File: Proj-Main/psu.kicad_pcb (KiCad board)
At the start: 2 copper layers, 100 x 75 mm, 124 parts, among them J1 METER, J3 T1A, J4 T1B, J5 T1C, J6 SENSE, J8 OUT+, J9 OUT-, Q1 BC856, Q10 BC856, Q11 PMP4201Y, Q12 MMBT3904, Q13 BC856, Q14 MMBT3904, Q15 PZT2222A, Q16 MMBT3904, Q17 TIP105, Q18 PMP4201Y, Q19 MMBT2907A, Q2 MMBT3904, Q20 MMBT2907A, Q21 MMBT2907A, Q22 MMBT3904, Q23 PMP4201Y, Q24 MMBT3904, Q3 PZT2222A, Q4 BC856, Q5 MMBT3906, Q6 MMBT3906, Q7 PMP4201Y, Q8 PMP4201Y, Q9 BC856

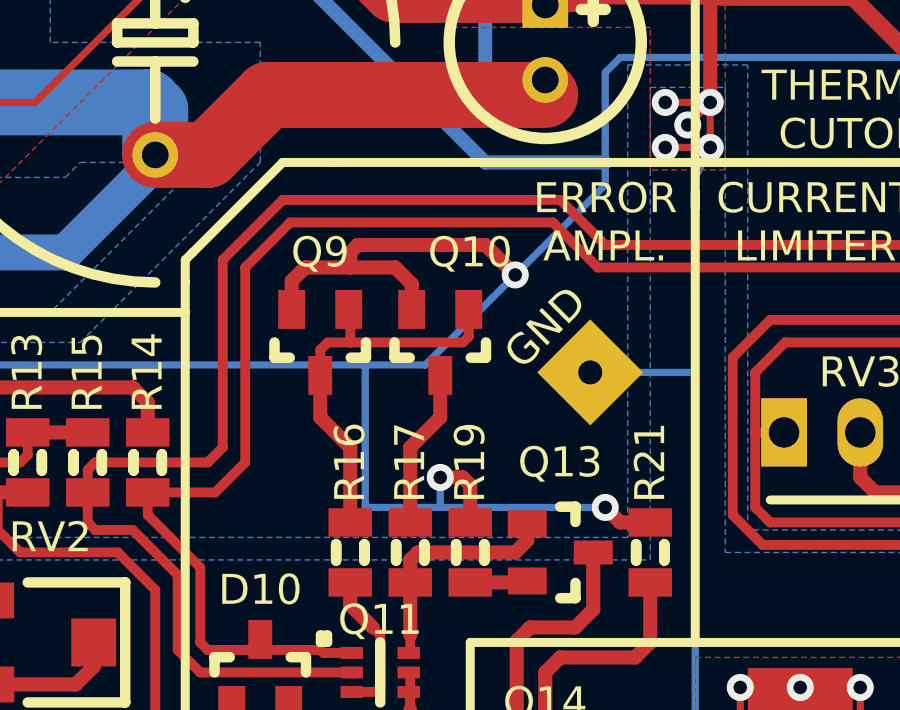
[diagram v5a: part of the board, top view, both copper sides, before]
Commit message: Added current mirror degeneration resistors R54, R55
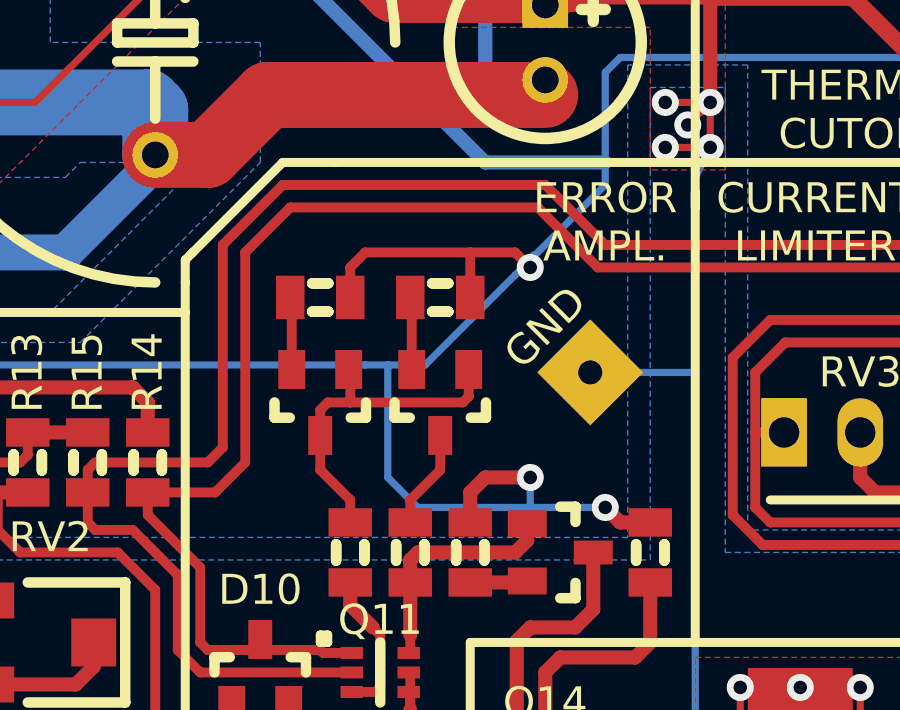
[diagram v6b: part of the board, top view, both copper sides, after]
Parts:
- added R54: 100, IPC7351-Nominal:RESC2012X50, F.Cu at (160.0, 86.5)
- added R55: 100, IPC7351-Nominal:RESC2012X50, F.Cu at (164.0, 86.5)
- moved Q10 2.00 mm to (164.0, 90.0)
- moved Q9 2.00 mm to (160.0, 90.0)
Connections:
- Q10 pad 2: V+ -> Net-(Q10-Pad2)
- Q9 pad 2: V+ -> Net-(Q9-Pad2)
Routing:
- net V+: track 278.0 -> 273.6 mm
- net Net-(Q9-Pad2): track 0.00 -> 2.42 mm
- net Net-(Q10-Pad2): track 0.00 -> 2.42 mm
- net Net-(Q10-Pad1): track 13.4 -> 11.3 mm
- net Net-(Q10-Pad3): track 5.31 -> 3.31 mm
- net /FB+: track 95.1 -> 95.8 mm
- net /FB-: track 89.5 -> 90.2 mm

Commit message: Renamed voltage rails (V+ and V- now +2 and -12)
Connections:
- net V+ renamed +2
- net V- renamed -12
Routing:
- added copper zone on B.Cu, net V+
- added copper zone on F.Cu, net V+
- added copper zone on B.Cu, net V-
- added copper zone on F.Cu, net V-
- removed copper zone on B.Cu, net +2
- removed copper zone on F.Cu, net +2
- removed copper zone on B.Cu, net -12
- removed copper zone on F.Cu, net -12

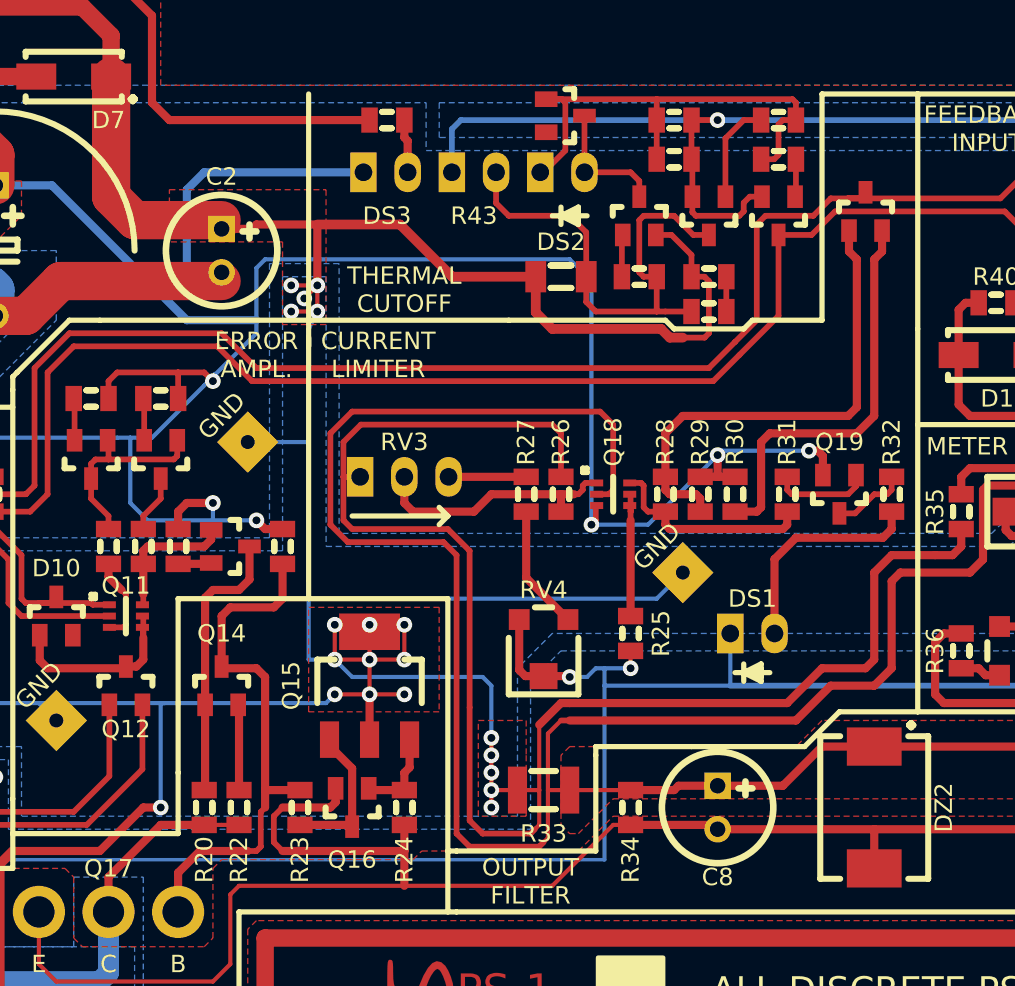
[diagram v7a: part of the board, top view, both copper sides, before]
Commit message: Updated LED bias points
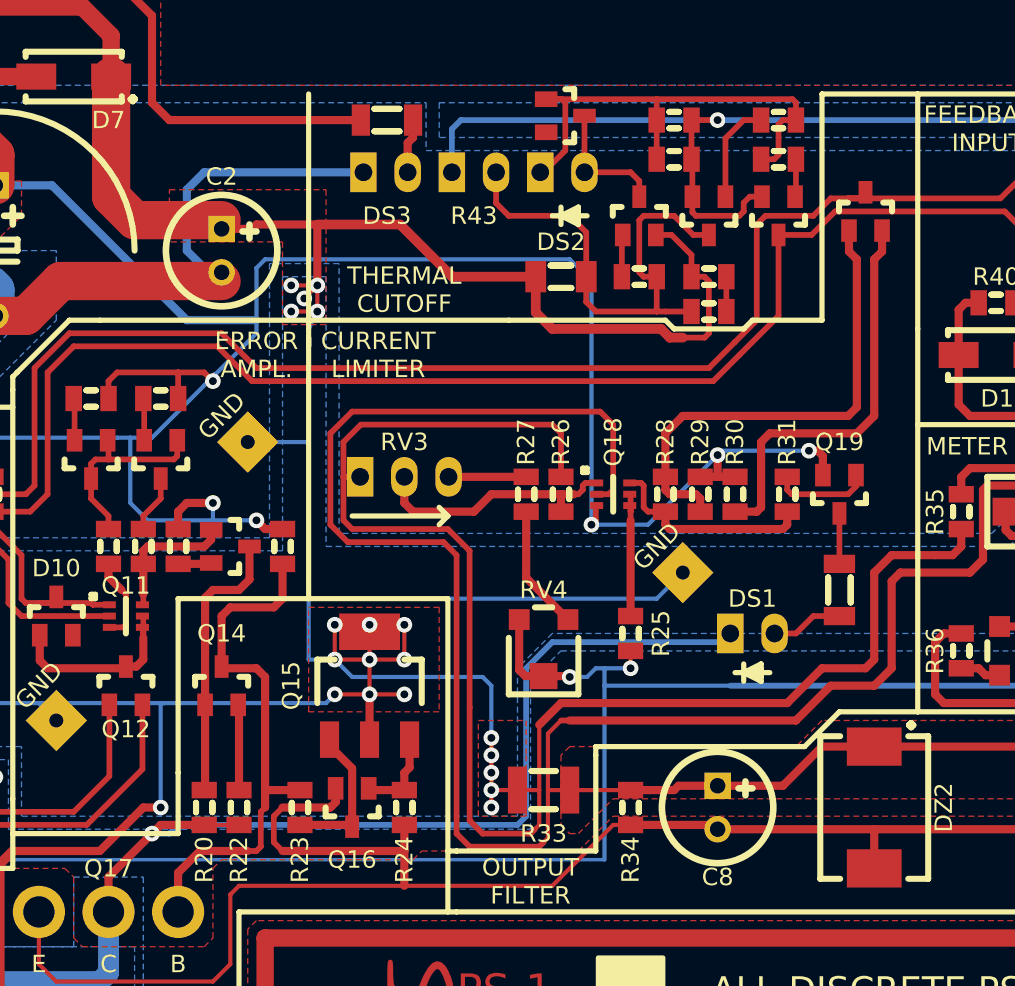
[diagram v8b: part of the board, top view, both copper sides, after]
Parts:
- R2, R32: value 10k -> 10k QW; footprint IPC7351-Nominal:RESC2012X50 -> IPC7351-Nominal:RESC3216X60
- moved R32 6.26 mm to (203.0, 97.5)
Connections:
- DS1 pad K: -12 -> V-UNREG
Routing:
- net V-UNREG: track 200.8 -> 243.2 mm, vias 1 -> 2
- net Net-(DS1-PadA): track 12.7 -> 4.17 mm
- net -12: track 282.0 -> 279.0 mm
- net Net-(Q19-Pad3): track 4.31 -> 2.90 mm
- net +2: track 273.6 -> 273.1 mm
- added copper zone on B.Cu, net +2
- added copper zone on B.Cu, net -12
- removed copper zone on B.Cu, net V+
- removed copper zone on B.Cu, net V-
